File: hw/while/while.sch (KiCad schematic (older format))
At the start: 22 parts, among them J1 conn_trigger, J2 conn_done, J3 FTDI, J4 conn_active, J5 conn_condition, J6 cond_select, SW2 switch_active, SW3 switch_reset, U1 ATmega328P-PU, Y1 Crystal

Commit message: update hardware
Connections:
- net GND: no longer H1.1, H2.1, H3.1, H4.1
- net at SW2.3: no longer SW2.4
- net at SW3.3: no longer SW3.4
- no-connect marks 12 -> 20
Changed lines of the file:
@@
 a4
-Wire Wire Line
-	9450 2900 9400 2900
-Wire Wire Line
-	9400 2900 9400 3000
-Wire Wire Line
-	9400 3000 9850 3000
-Wire Wire Line
-	9850 3000 9850 2900
-Wire Wire Line
-	4250 2900 4250 3000
-Wire Wire Line
-	4250 3000 4750 3000
-Wire Wire Line
-	4300 2900 4250 2900
-Wire Wire Line
-	4700 2900 4750 2900
-Wire Wire Line
-	4750 2900 4750 3000
 Wire Wire Line
 	4450 4150 4650 4150
@@
 $EndComp
 $Comp
-L power:GND #PWR024
-U 1 1 5BCCEE7F
-P 1250 5850
-F 0 "#PWR024" H 1250 5600 50  0001 C CNN
-F 1 "GND" H 1255 5677 50  0000 C CNN
-F 2 "" H 1250 5850 50  0001 C CNN
-F 3 "" H 1250 5850 50  0001 C CNN
-	1    1250 5850
-	1    0    0    -1
-$EndComp
-Wire Wire Line
-	1000 5550 1000 5700
-Wire Wire Line
-	1000 5700 1250 5700
-Wire Wire Line
-	1400 5700 1400 5550
-Wire Wire Line
-	1250 5850 1250 5700
-Connection ~ 1250 5700
-Wire Wire Line
-	1250 5700 1400 5700
-$Comp
 L Mechanical:MountingHole_Pad H3
 U 1 1 5BCDCAFD
@@
 	1    0    0    -1
 $EndComp
-Wire Wire Line
-	1750 5550 1750 5700
-Wire Wire Line
-	1750 5700 1400 5700
-Connection ~ 1400 5700
 $Comp
 L Mechanical:MountingHole_Pad H4
@@
 	1    0    0    -1
 $EndComp
-Wire Wire Line
-	700  5550 700  5700
-Wire Wire Line
-	700  5700 1000 5700
-Connection ~ 1000 5700
 $Comp
 L Connector:Conn_01x03_Male J5
@@
 	1    0    0    -1
 $EndComp
+NoConn ~ 700  5550
+NoConn ~ 1000 5550
+NoConn ~ 1400 5550
+NoConn ~ 1750 5550
+NoConn ~ 4700 2900
+NoConn ~ 4300 2900
+NoConn ~ 9850 2900
+NoConn ~ 9450 2900
 $EndSCHEMATC

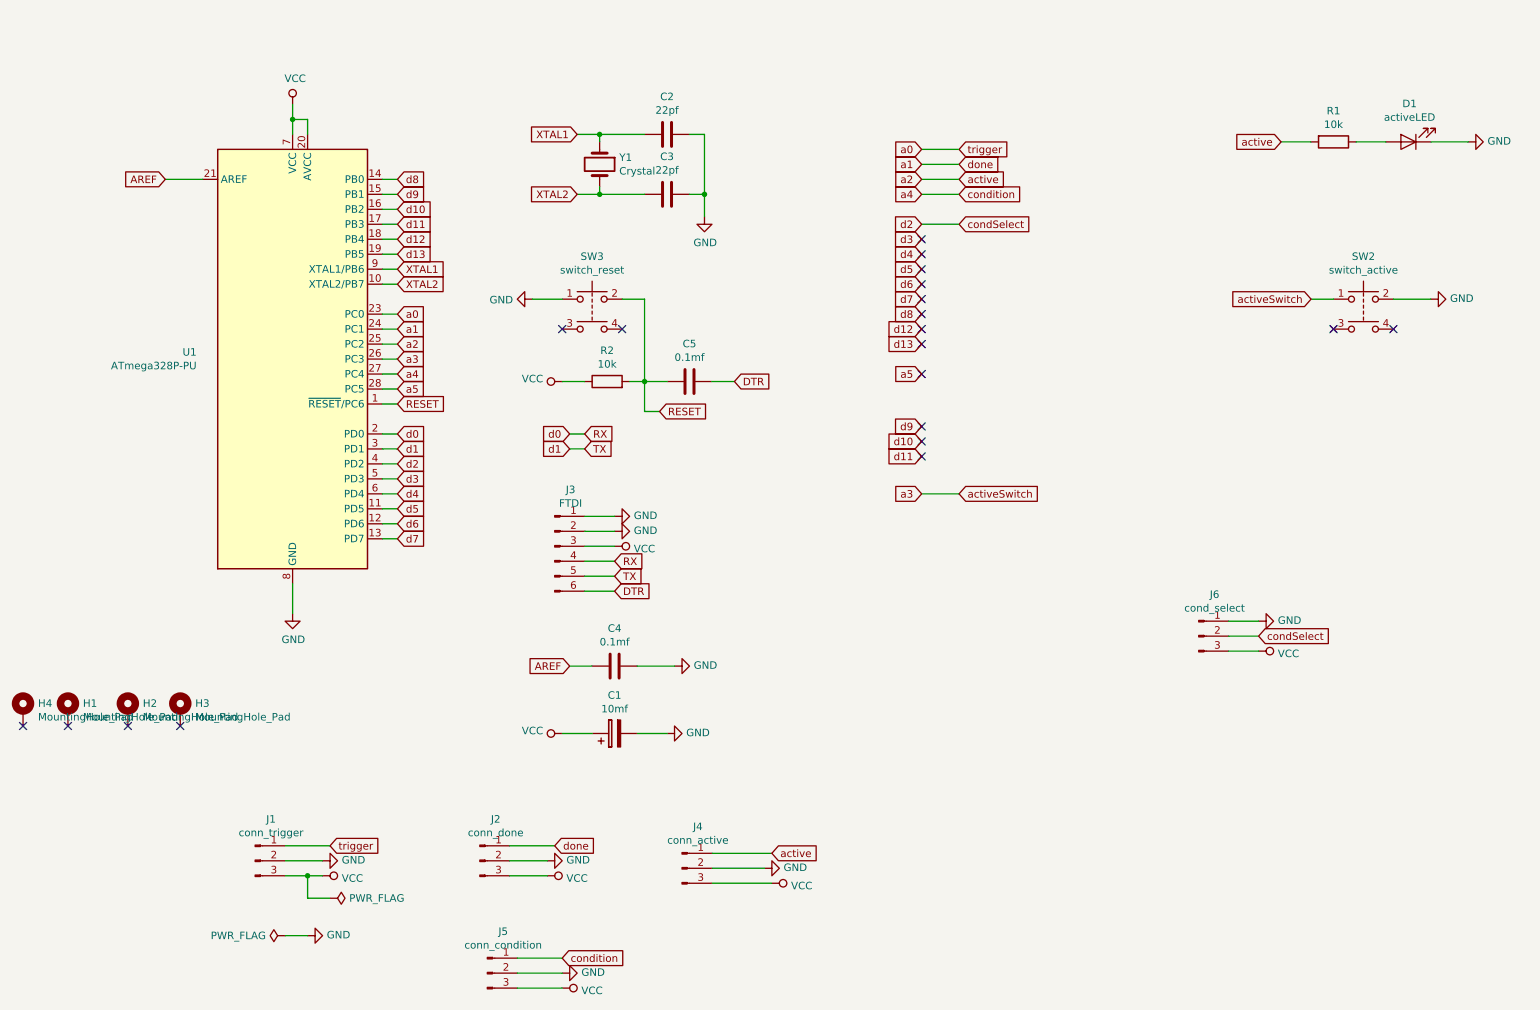
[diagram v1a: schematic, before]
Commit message: WHILE block v2
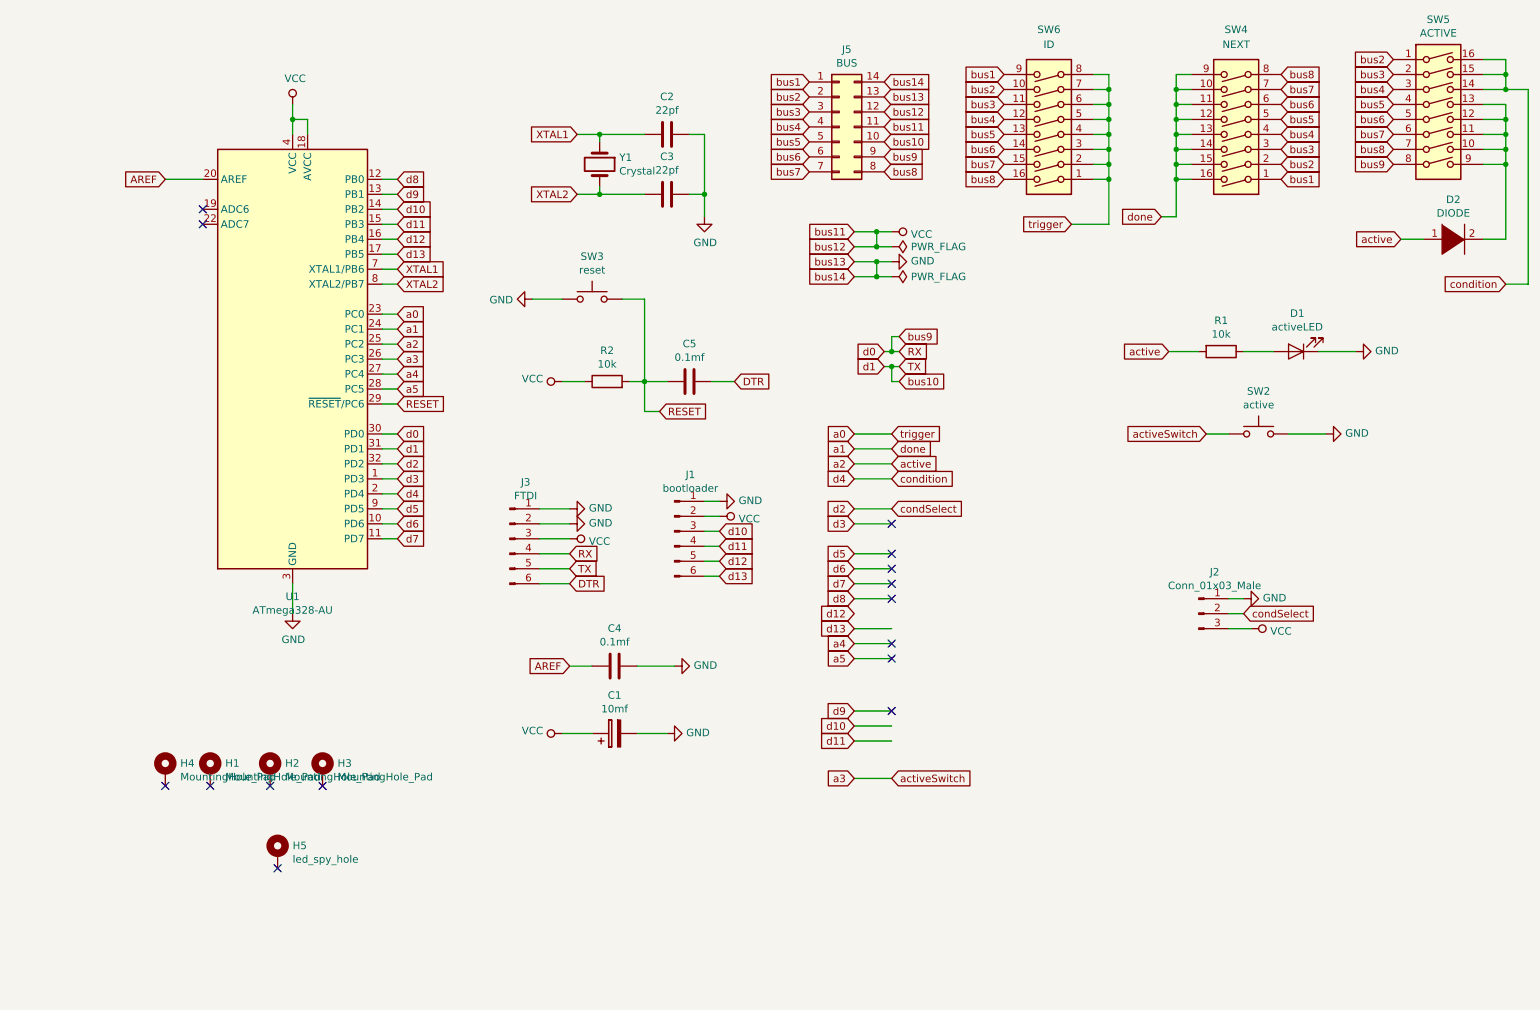
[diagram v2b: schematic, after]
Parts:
- removed J1: conn_trigger, Connector_PinHeader_2.54mm:PinHeader_1x03_P2.54mm_Vertical, symbol Connector:Conn_01x03_Male
- removed J4: conn_active, Connector_PinHeader_2.54mm:PinHeader_1x03_P2.54mm_Vertical, symbol Connector:Conn_01x03_Male
- removed J5: conn_condition, Connector_PinHeader_2.54mm:PinHeader_1x03_P2.54mm_Vertical, symbol Connector:Conn_01x03_Male
- removed J6: cond_select, Connector_PinHeader_2.54mm:PinHeader_1x03_P2.54mm_Vertical, symbol Connector:Conn_01x03_Male
- removed SW2: switch_active, autoblocks:SW_PUSH_6mm_H5mm, symbol Switch:SW_Push_Dual
- removed SW3: switch_reset, autoblocks:SW_PUSH_6mm_H5mm, symbol Switch:SW_Push_Dual
- removed U1: ATmega328P-PU, Package_DIP:DIP-28_W7.62mm, symbol MCU_Microchip_ATmega:ATmega328P-PU
- added D2: DIODE, Diode_SMD:D_0603_1608Metric, symbol pspice:DIODE
- added H5: led_spy_hole, MountingHole:MountingHole_3.2mm_M3, symbol Mechanical:MountingHole_Pad
- added J1: bootloader, autoblocks:edge_connector_3, symbol Connector:Conn_01x06_Male
- added J5: BUS, Connector_PinHeader_2.54mm:PinHeader_2x07_P2.54mm_Vertical, symbol Connector_Generic:Conn_02x07_Counter_Clockwise
- added SW2: active, Button_Switch_SMD:SW_SPST_TL3305C, symbol Switch:SW_Push
- added SW3: reset, Button_Switch_SMD:SW_SPST_TL3305C, symbol Switch:SW_Push
- added SW4: NEXT, Package_DIP:DIP-16_W7.62mm_SMDSocket_SmallPads, symbol Switch:SW_DIP_x08
- added SW5: ACTIVE, Package_DIP:DIP-16_W7.62mm_SMDSocket_SmallPads, symbol Switch:SW_DIP_x08
- added SW6: ID, Package_DIP:DIP-16_W7.62mm_SMDSocket_SmallPads, symbol Switch:SW_DIP_x08
- added U1: ATmega328-AU, Package_QFP:TQFP-32_7x7mm_P0.8mm, symbol MCU_Microchip_ATmega:ATmega328-AU
- C1: footprint Capacitor_THT:CP_Radial_Tantal_D6.0mm_P2.50mm -> Capacitor_SMD:C_0603_1608Metric
- C2, C3: footprint Capacitor_THT:C_Disc_D3.0mm_W1.6mm_P2.50mm -> Capacitor_SMD:C_0603_1608Metric
- C4, C5: footprint Capacitor_THT:C_Axial_L5.1mm_D3.1mm_P7.50mm_Horizontal -> Capacitor_SMD:C_0603_1608Metric
- H1, H2, H3, H4: footprint MountingHole:MountingHole_2.2mm_M2 -> MountingHole:MountingHole_3.2mm_M3_Pad
- J2: value conn_done -> Conn_01x03_Male
- J3: footprint Connector_PinHeader_2.54mm:PinHeader_1x06_P2.54mm_Vertical -> autoblocks:edge_connector_3
- R1, R2: footprint Resistor_THT:R_Axial_DIN0207_L6.3mm_D2.5mm_P10.16mm_Horizontal -> Resistor_SMD:R_0603_1608Metric
- Y1: footprint Crystal:Crystal_HC18-U_Vertical -> Crystal:Crystal_SMD_HC49-SD
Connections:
- net AREF: now also U1.20 (AREF)
- net GND: now also J2.1 (Pin_1), J1.1 (Pin_1), J5.13 (Pin_13), J5.14 (Pin_14), SW2.2, SW3.1, U1.21 (GND), U1.3 (GND), U1.5 (GND); no longer J2.2 (Pin_2)
- net RESET: now also SW3.2, U1.29 (~RESET~/PC6)
- net RX: now also J5.9 (Pin_9), SW5.8, U1.30 (PD0)
- net TX: now also J5.10 (Pin_10), U1.31 (PD1)
- net VCC: now also J1.2 (Pin_2), J5.11 (Pin_11), J5.12 (Pin_12), U1.18 (AVCC), U1.4 (VCC), U1.6 (VCC)
- net XTAL1: now also U1.7 (XTAL1/PB6)
- net XTAL2: now also U1.8 (XTAL2/PB7)
- net a0: now also SW6.1, SW6.2, SW6.3, SW6.4, SW6.5, SW6.6, SW6.7, SW6.8, U1.23 (PC0)
- net a1: now also SW4.10, SW4.11, SW4.12, SW4.13, SW4.14, SW4.15, SW4.16, SW4.9, U1.24 (PC1); no longer J2.1 (Pin_1)
- net a2: now also D2.1 (K), U1.25 (PC2)
- net a3: now also SW2.1, U1.26 (PC3)
- net a4: now also U1.27 (PC4)
- net a5: now also U1.28 (PC5)
- net condSelect: now also J2.2 (Pin_2), U1.32 (PD2)
- net d10: now also J1.3 (Pin_3), U1.14 (PB2)
- net d11: now also J1.4 (Pin_4), U1.15 (PB3)
- net d12: now also J1.5 (Pin_5), U1.16 (PB4)
- net d13: now also J1.6 (Pin_6), U1.17 (PB5)
- net d3: now also U1.1 (PD3)
- net d5: now also U1.9 (PD5)
- net d6: now also U1.10 (PD6)
- net d7: now also U1.11 (PD7)
- net d8: now also U1.12 (PB0)
- net d9: now also U1.13 (PB1)
- new net: D2.2 (A), SW5.10, SW5.11, SW5.12, SW5.13, SW5.9
- new net bus1: J5.1 (Pin_1), SW4.1, SW6.9
- new net bus2: J5.2 (Pin_2), SW4.2, SW5.1, SW6.10
- new net bus3: J5.3 (Pin_3), SW4.3, SW5.2, SW6.11
- new net bus4: J5.4 (Pin_4), SW4.4, SW5.3, SW6.12
- new net bus5: J5.5 (Pin_5), SW4.5, SW5.4, SW6.13
- new net bus6: J5.6 (Pin_6), SW4.6, SW5.5, SW6.14
- new net bus7: J5.7 (Pin_7), SW4.7, SW5.6, SW6.15
- new net bus8: J5.8 (Pin_8), SW4.8, SW5.7, SW6.16
- new net condition: SW5.14, SW5.15, SW5.16, U1.2 (PD4)
- no-connect marks 20 -> 15
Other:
- moved on the sheet: D1, H2, H3, J3, R1

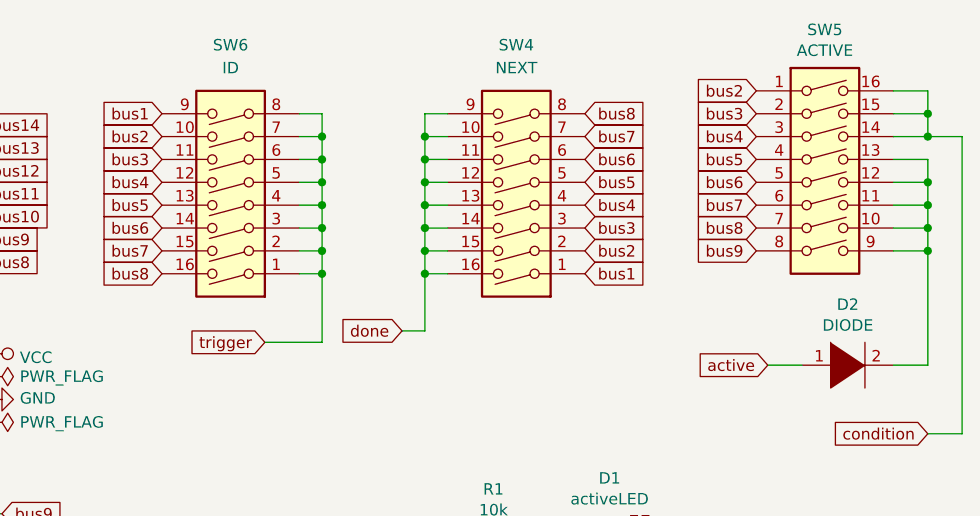
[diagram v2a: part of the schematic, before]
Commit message: fix WHILE bus assignemnts
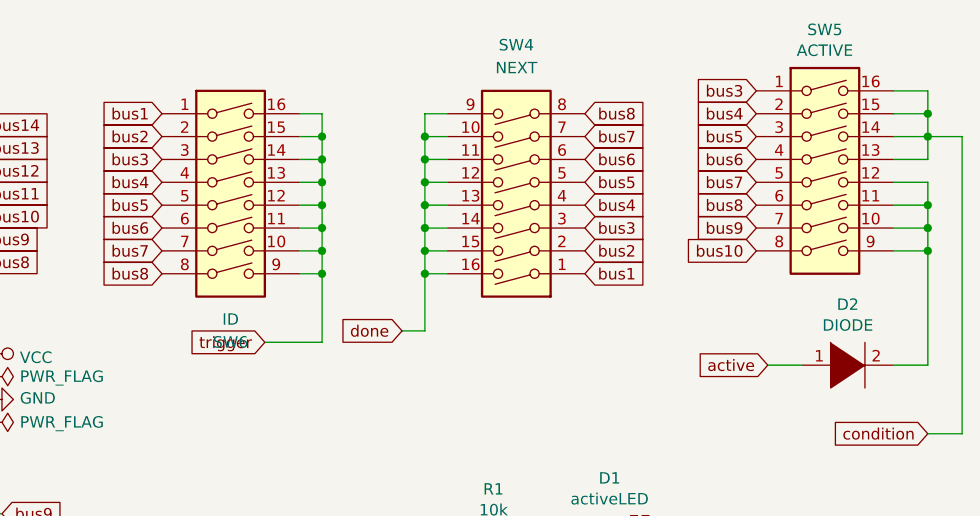
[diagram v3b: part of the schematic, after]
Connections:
- net RX: now also SW5.7; no longer SW5.8
- net TX: now also SW5.8
- net a0: now also SW6.10, SW6.11, SW6.12, SW6.13, SW6.14, SW6.15, SW6.16, SW6.9; no longer SW6.1, SW6.2, SW6.3, SW6.4, SW6.5, SW6.6, SW6.7, SW6.8
- net bus1: now also SW6.1; no longer SW6.9
- net bus2: now also SW6.2; no longer SW5.1, SW6.10
- net bus3: now also SW5.1, SW6.3; no longer SW5.2, SW6.11
- net bus4: now also SW5.2, SW6.4; no longer SW5.3, SW6.12
- net bus5: now also SW5.3, SW6.5; no longer SW5.4, SW6.13
- net bus6: now also SW5.4, SW6.6; no longer SW5.5, SW6.14
- net bus7: now also SW5.5, SW6.7; no longer SW5.6, SW6.15
- net bus8: now also SW5.6, SW6.8; no longer SW5.7, SW6.16
- net condition: now also SW5.13
- net at D2.2 (A), SW5.10, SW5.11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: no longer SW5.13
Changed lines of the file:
@@
 $EndComp
 Text GLabel 9850 1100 0    50   Input ~ 0
-bus2
+bus3
 Text GLabel 9850 1200 0    50   Input ~ 0
-bus3
+bus4
 Text GLabel 9850 1300 0    50   Input ~ 0
-bus4
+bus5
 Text GLabel 9850 1400 0    50   Input ~ 0
-bus5
+bus6
 Text GLabel 9850 1500 0    50   Input ~ 0
-bus6
+bus7
 Text GLabel 9850 1600 0    50   Input ~ 0
-bus7
+bus8
 Text GLabel 9850 1700 0    50   Input ~ 0
-bus8
-Text GLabel 9850 1800 0    50   Input ~ 0
 bus9
 Wire Wire Line
@@
 L Switch:SW_DIP_x08 SW6
 U 1 1 5C35B265
-P 7550 1500
-F 0 "SW6" H 7550 900 50  0000 C CNN
-F 1 "ID" H 7550 1000 50  0000 C CNN
-F 2 "Package_DIP:DIP-16_W7.62mm_SMDSocket_SmallPads" H 7550 1500 50  0001 C CNN
-F 3 "" H 7550 1500 50  0001 C CNN
-	1    7550 1500
-	-1   0    0    1
+P 7550 1600
+F 0 "SW6" H 7550 1000 50  0000 C CNN
+F 1 "ID" H 7550 1100 50  0000 C CNN
+F 2 "Package_DIP:DIP-16_W7.62mm_SMDSocket_SmallPads" H 7550 1600 50  0001 C CNN
+F 3 "" H 7550 1600 50  0001 C CNN
+	1    7550 1600
+	1    0    0    -1
 $EndComp
 $Comp
@@
 Wire Wire Line
 	10450 1400 10600 1400
-Wire Wire Line
-	10600 1400 10600 1500
-Connection ~ 10600 1500
+Text GLabel 9850 1800 0    50   Input ~ 0
+bus10
+Wire Wire Line
+	10600 1300 10600 1400
 $EndSCHEMATC
